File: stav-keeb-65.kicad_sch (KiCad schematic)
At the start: 0 parts

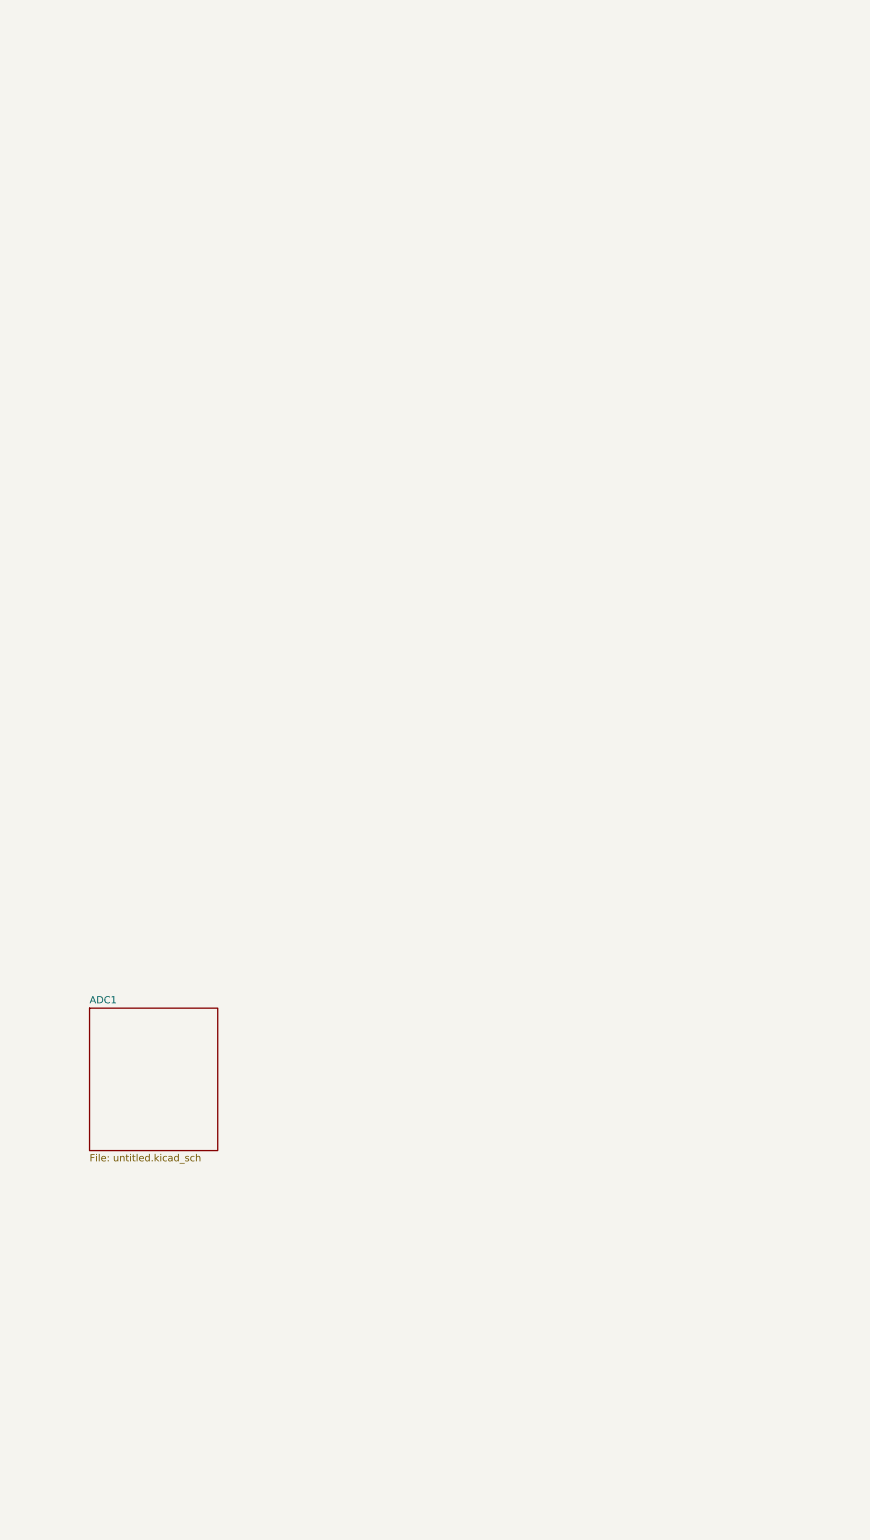
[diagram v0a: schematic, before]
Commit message: RP2040 initial draw
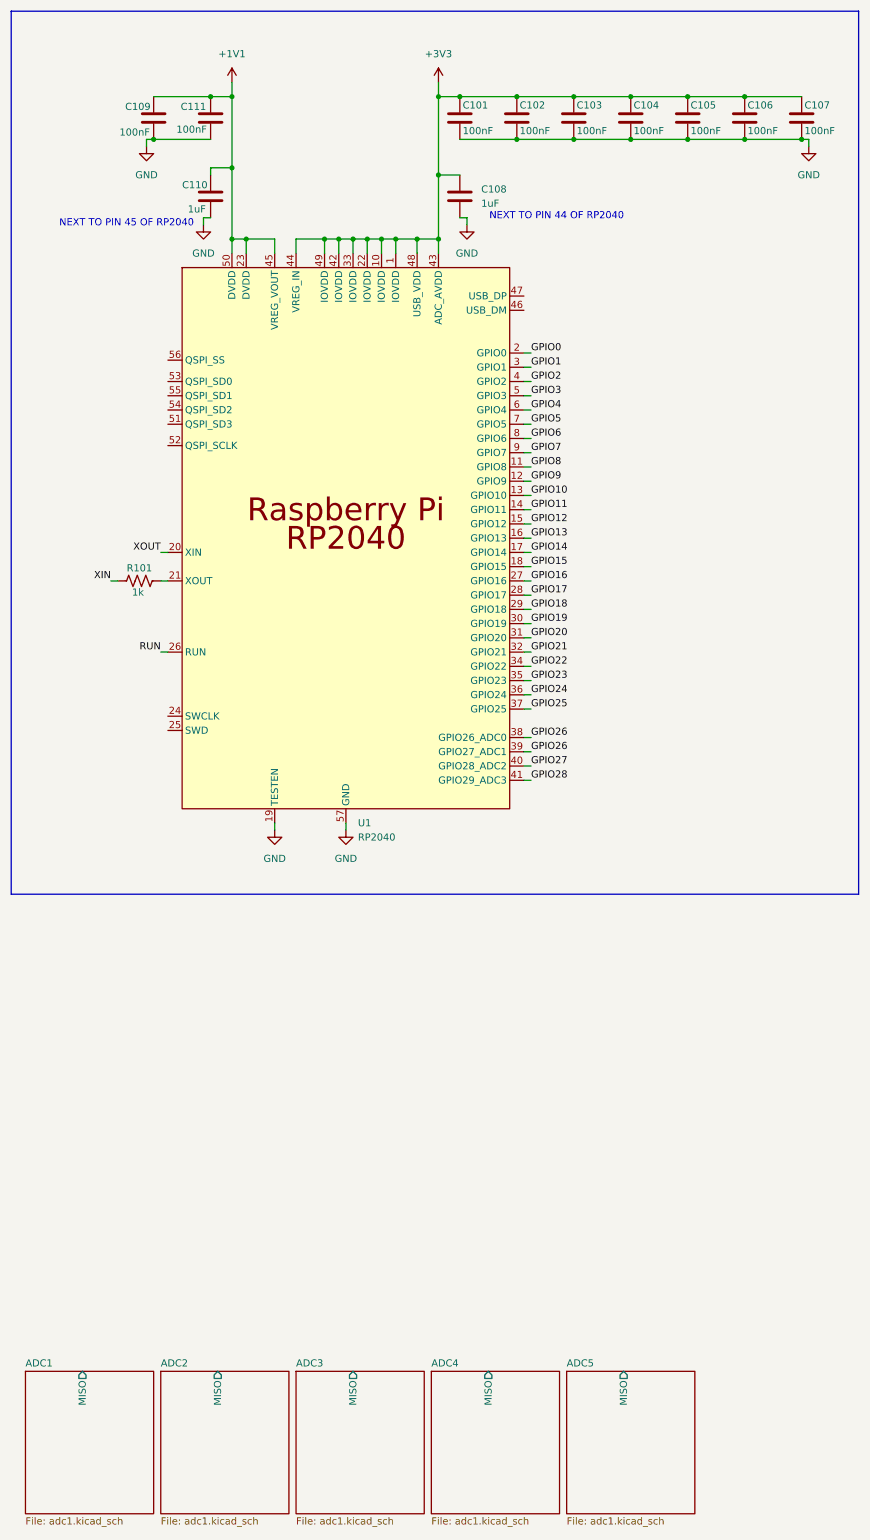
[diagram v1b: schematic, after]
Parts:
- added C101, C102, C103, C104, C105, C106, C107, C109, C111: 100nF, Capacitor_SMD:C_0201_0603Metric_Pad0.64x0.40mm_HandSolder, symbol Device:C
- added C108, C110: 1uF, Capacitor_SMD:C_0201_0603Metric_Pad0.64x0.40mm_HandSolder, symbol Device:C
- added R101: 1k, Capacitor_SMD:C_0201_0603Metric_Pad0.64x0.40mm_HandSolder, symbol Device:R_US
- added U1: RP2040, easyeda2kicad:LQFN-56_L7.0-W7.0-P0.4-EP, symbol easyeda2kicad:RP2040
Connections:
- new net: R101.2, U1.21 (XOUT)
- new net +1V1: C109.1, C110.1, C111.1, U1.23 (DVDD), U1.45 (VREG_VOUT), U1.50 (DVDD)
- new net +3V3: C101.1, C102.1, C103.1, C104.1, C105.1, C106.1, C107.1, C108.1, U1.1 (IOVDD), U1.10 (IOVDD), U1.22 (IOVDD), U1.33 (IOVDD), U1.42 (IOVDD), U1.43 (ADC_AVDD), U1.44 (VREG_IN), U1.48 (USB_VDD), U1.49 (IOVDD)
- new net GND: C101.2, C102.2, C103.2, C104.2, C105.2, C106.2, C107.2, C108.2, C109.2, C110.2, C111.2, U1.19 (TESTEN), U1.57 (GND)
- new net GPIO0: U1.2 (GPIO0)
- new net GPIO1: U1.3 (GPIO1)
- new net GPIO10: U1.13 (GPIO10)
- new net GPIO11: U1.14 (GPIO11)
- new net GPIO12: U1.15 (GPIO12)
- new net GPIO13: U1.16 (GPIO13)
- new net GPIO14: U1.17 (GPIO14)
- new net GPIO15: U1.18 (GPIO15)
- new net GPIO16: U1.27 (GPIO16)
- new net GPIO17: U1.28 (GPIO17)
- new net GPIO18: U1.29 (GPIO18)
- new net GPIO19: U1.30 (GPIO19)
- new net GPIO2: U1.4 (GPIO2)
- new net GPIO20: U1.31 (GPIO20)
- new net GPIO21: U1.32 (GPIO21)
- new net GPIO22: U1.34 (GPIO22)
- new net GPIO23: U1.35 (GPIO23)
- new net GPIO24: U1.36 (GPIO24)
- new net GPIO25: U1.37 (GPIO25)
- new net GPIO26: U1.38 (GPIO26_ADC0), U1.39 (GPIO27_ADC1)
- new net GPIO27: U1.40 (GPIO28_ADC2)
- new net GPIO28: U1.41 (GPIO29_ADC3)
- new net GPIO3: U1.5 (GPIO3)
- new net GPIO4: U1.6 (GPIO4)
- new net GPIO5: U1.7 (GPIO5)
- new net GPIO6: U1.8 (GPIO6)
- new net GPIO7: U1.9 (GPIO7)
- new net GPIO8: U1.11 (GPIO8)
- new net GPIO9: U1.12 (GPIO9)
- new net RUN: U1.26 (RUN)
- new net XIN: R101.1
- new net XOUT: U1.20 (XIN)
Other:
- added sheet ADC2 (adc1.kicad_sch)
- added sheet ADC3 (adc1.kicad_sch)
- added sheet ADC4 (adc1.kicad_sch)
- added sheet ADC5 (adc1.kicad_sch)
- sheet ADC1: file untitled.kicad_sch -> adc1.kicad_sch
- sheet ADC1 ports: added MISO; removed none
- note added: "NEXT TO PIN 44 OF RP2040"
- note added: "NEXT TO PIN 45 OF RP2040"
- title: (none) -> stav-keeb-65

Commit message: Oscillator and Flash
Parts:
- added C112: 100nF, Capacitor_SMD:C_0201_0603Metric_Pad0.64x0.40mm_HandSolder, symbol Device:C
- added C113, C114: 20pF, Capacitor_SMD:C_0201_0603Metric_Pad0.64x0.40mm_HandSolder, symbol Device:C
- added C115: 1uF, Capacitor_SMD:C_0201_0603Metric_Pad0.64x0.40mm_HandSolder, symbol Device:C
- added R102: 10k, Resistor_SMD:R_0201_0603Metric_Pad0.64x0.40mm_HandSolder, symbol Device:R_US
- added U7: ZD25D40CNJGR, easyeda2kicad:USON-8_L1.5-W1.5-P0.40-BL-EP, symbol easyeda2kicad:ZD25D40CNJGR
- added X1: X322512MSB4SI, easyeda2kicad:CRYSTAL-SMD_4P-L3.2-W2.5-BL, symbol easyeda2kicad:X322512MSB4SI
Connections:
- net +3V3: now also C115.1, R102.1
- net GND: now also C112.2, C113.2, C114.1, U7.4 (GND), U7.9 (EP), X1.2 (GND), X1.4 (GND)
- net RUN: now also C112.1, R102.2
- net XIN: now also C113.1, X1.3 (OSC2)
- net XOUT: now also C114.2, X1.1 (OSC1)
- net FLASH_SCLK: now reaches U1.52 (QSPI_SCLK)
- net FLASH_SCLK: now also U7.6 (SCLK)
- net FLASH_SD0: now reaches U1.53 (QSPI_SD0)
- net FLASH_SD0: now also U7.5 (SI)
- net FLASH_SD2: now reaches U1.54 (QSPI_SD2)
- net FLASH_SD2: now also U7.3 (~{WP})
- net FLASH_SD1: now reaches U1.55 (QSPI_SD1)
- net FLASH_SD1: now also U7.2 (SO)
- net FLASH_~{CS}: now reaches U1.56 (QSPI_SS)
- net FLASH_~{CS}: now also U7.1 (~{CS})
- new net: C115.2, U7.8 (VCC)
- no-connect marks 0 -> 2
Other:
- note added: "DO NOT POOR COPPER"

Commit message: RESET & BOOTSEL BUTTONS
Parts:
- added SW201: RESET, easyeda2kicad:SW-SMD_4P-L5.1-W5.1-P3.70-LS6.5-TL_H1.5, symbol easyeda2kicad:TS-1187A-B-A-B
- added SW202: BOOTSEL, easyeda2kicad:SW-SMD_4P-L5.1-W5.1-P3.70-LS6.5-TL_H1.5, symbol easyeda2kicad:TS-1187A-B-A-B
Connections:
- net FLASH_~{CS}: now also SW202.1 (A), SW202.2 (B)
- net GND: now also SW201.3 (C), SW201.4 (D), SW202.3 (C), SW202.4 (D)
- net RUN: now also SW201.1 (A), SW201.2 (B)

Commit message: Power & USB
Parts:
- added C116, C119, C120: 100nF, Capacitor_SMD:C_0603_1608Metric_Pad1.08x0.95mm_HandSolder, symbol Device:C
- added C117, C118: 10uF, Capacitor_SMD:C_1206_3216Metric_Pad1.33x1.80mm_HandSolder, symbol Device:C
- added C121: 22uF, Capacitor_SMD:C_1206_3216Metric_Pad1.33x1.80mm_HandSolder, symbol Device:C
- added C122: 4.7nF, Capacitor_SMD:C_0603_1608Metric_Pad1.08x0.95mm_HandSolder, symbol Device:C
- added C123, C124: 1nF, Capacitor_SMD:C_0603_1608Metric_Pad1.08x0.95mm_HandSolder, symbol Device:C
- added D1: SMF5.0A, easyeda2kicad:SOD-123F_L2.8-W1.8-LS3.7-RD, symbol easyeda2kicad:SMF5.0A_C151296
- added D2: USBLC6-2SC6, easyeda2kicad:SOT-23-6_L2.9-W1.6-P0.95-LS2.8-BL, symbol easyeda2kicad:USBLC6-2SC6
- added F1: Littelfuse 1812L110/33MR, symbol Device:Fuse
- added FB1: TDK MPZ2012S101AT000, symbol Device:FerriteBead
- added R103, R104: 5.1k, Resistor_SMD:R_0603_1608Metric_Pad0.98x0.95mm_HandSolder, symbol Device:R_US
- added R105: 1M, Resistor_SMD:R_0603_1608Metric_Pad0.98x0.95mm_HandSolder, symbol Device:R_US
- added R106, R107: 100k, Resistor_SMD:R_0603_1608Metric_Pad0.98x0.95mm_HandSolder, symbol Device:R_US
- added U8: RT9013-33GB, easyeda2kicad:SOT-23-5_L3.0-W1.7-P0.95-LS2.8-BL, symbol easyeda2kicad:RT9013-33GB
- added USBC1: TYPE-C-31-M-12, easyeda2kicad:USB-C_SMD-TYPE-C-31-M-12_1, symbol easyeda2kicad:TYPE-C-31-M-12
- C101, C102, C103, C104, C105, C106, C107, C108, C109, C110, C111, C112, C113, C114, C115, R101: footprint Capacitor_SMD:C_0201_0603Metric_Pad0.64x0.40mm_HandSolder -> Capacitor_SMD:C_0603_1608Metric_Pad1.08x0.95mm_HandSolder
- R102: footprint Resistor_SMD:R_0201_0603Metric_Pad0.64x0.40mm_HandSolder -> Capacitor_SMD:C_0603_1608Metric_Pad1.08x0.95mm_HandSolder
- renumbered SW201 to _SW201, SW202 to _SW202
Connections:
- net +3V3: now also C116.1, C117.1, U8.5 (VOUT)
- net GND: now also C116.2, C117.2, C118.2, C119.2, C120.2, C121.2, C122.2, C123.1, C124.2, D1.2, D2.2, R103.2, R105.2, U8.2 (GND), USBC1.A1B12 (GND), USBC1.B1A12 (GND)
- net GPIO26: now also C123.2, R107.1; no longer U1.39 (GPIO27_ADC1)
- net GPIO27: now also U1.39 (GPIO27_ADC1), C124.1, R106.1; no longer U1.40 (GPIO28_ADC2)
- net GPIO28: now also U1.40 (GPIO28_ADC2); no longer U1.41 (GPIO29_ADC3)
- new net: R103.1, R107.2, USBC1.A5 (CC1)
- new net: R104.1, R106.2, USBC1.B5 (CC2)
- new net: C122.1, R105.1, USBC1.1 (EH), USBC1.2 (EH), USBC1.3 (EH), USBC1.4 (EH)
- new net GPIO29: U1.41 (GPIO29_ADC3)
- new net USB_D1N: D2.3, USBC1.A7 (DN1), USBC1.B7 (DN2)
- new net USB_D1P: D2.1, USBC1.A6 (DP1), USBC1.B6 (DP2)
- new net USB_DN: D2.4
- new net USB_DP: D2.6
- new net VBUS: D1.1, D2.5, F1.1, USBC1.A4B9 (VBUS), USBC1.B4A9 (VBUS)
- new net V_Filtered: C120.1, C121.1, FB1.2
- new net V_Fused: C118.1, C119.1, F1.2, FB1.1, U8.1 (VIN), U8.3 (EN)
- no-connect marks 2 -> 5

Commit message: USB connection to RP2040
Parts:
- added R108, R109: 22, Resistor_SMD:R_0603_1608Metric_Pad0.98x0.95mm_HandSolder, symbol Device:R_US
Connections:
- net USB_DN: now also R109.1
- net USB_DP: now also R108.1
- net at U1.46 (USB_DN): now also R109.2
- net at U1.47 (USB_DP): now also R108.2

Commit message: 2.5V ref
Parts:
- added C125: 10nF, Capacitor_SMD:C_0603_1608Metric_Pad1.08x0.95mm_HandSolder, symbol Device:C
- added C126: 1uF, Capacitor_SMD:C_0603_1608Metric_Pad1.08x0.95mm_HandSolder, symbol Device:C
- added C127, C129: 100nF, Capacitor_SMD:C_0603_1608Metric_Pad1.08x0.95mm_HandSolder, symbol Device:C
- added C128: 10uF, Capacitor_SMD:C_1206_3216Metric_Pad1.33x1.80mm_HandSolder, symbol Device:C
- added R110: 10, Resistor_SMD:R_0603_1608Metric_Pad0.98x0.95mm_HandSolder, symbol Device:R_US
- added R111, R112: 10k 0.1%, Resistor_SMD:R_0603_1608Metric_Pad0.98x0.95mm_HandSolder, symbol Device:R_US
- added U9: OPA320AIDBVR, easyeda2kicad:SOT-23-5_L3.0-W1.7-P0.95-LS2.8-BR, symbol easyeda2kicad:OPA320AIDBVR
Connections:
- net GND: now also C125.2, C126.2, C127.1, C128.2, C129.1, R112.2, U9.2 (V-)
- net V_Filtered renamed +5VA
- net +5VA: now also C126.1, C129.2, R111.1, U9.5 (V+)
- new net: C125.1, R111.2, R112.1, U9.3 (IN+)
- new net: R110.1, U9.1 (OUT), U9.4 (IN-)
- new net +2V5_RREF: C127.2, C128.1, R110.2
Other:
- note added: "ADC"
- note added: "Buttons"
- note added: "Flash"
- note added: "Microcontroller"
- note added: "Oscillator"
- note added: "Power"
- note added: "USB"

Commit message: Change 2.5V ref to voltage divider
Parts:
- removed U7: ZD25D40CNJGR, easyeda2kicad:USON-8_L1.5-W1.5-P0.40-BL-EP, symbol easyeda2kicad:ZD25D40CNJGR
- added C135: 100nF, Capacitor_SMD:C_0603_1608Metric_Pad1.08x0.95mm_HandSolder, symbol Device:C
- added R113: 1k, Resistor_SMD:R_0603_1608Metric_Pad0.98x0.95mm_HandSolder, symbol Device:R_US
- added R114: 10k, Resistor_SMD:R_0603_1608Metric_Pad0.98x0.95mm_HandSolder, symbol Device:R_US
- added U7: W25Q128JVSIQTR, easyeda2kicad:SOIC-8_L5.3-W5.3-P1.27-LS8.0-BL, symbol easyeda2kicad:W25Q128JVSIQTR
- R101, R102: footprint Capacitor_SMD:C_0603_1608Metric_Pad1.08x0.95mm_HandSolder -> Resistor_SMD:R_0603_1608Metric_Pad0.98x0.95mm_HandSolder
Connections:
- net +3V3: now also C135.1, R114.1
- net FLASH_SCLK: now also U7.6 (CLK)
- net FLASH_SD0: now also U7.5 (DI)
- net FLASH_SD1: now also U7.2 (DO)
- net FLASH_SD2: now also U7.3 (IO2)
- net FLASH_~{CS}: now also R113.1, R114.2, U7.1 (~{CS}); no longer _SW202.1 (A), _SW202.2 (B)
- net GND: now also U7.4 (GND)
- net at C115.2: now also C135.2, U7.8 (VCC)
- net FLASH_SD3: now reaches U1.51 (QSPI_SD3)
- net FLASH_SD3: now also U7.7 (IO3)
- new net: R113.2, _SW202.1 (A), _SW202.2 (B)
- no-connect marks 5 -> 3
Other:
- moved on the sheet: _SW201, _SW202

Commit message: ERC fixes
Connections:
- net GND: now also R104.2
- no-connect marks 3 -> 5
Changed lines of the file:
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@@
+	)
+	(no_connect
+		(at 40.64 140.97)
 	)
 	(no_connect
@@
 		(at 287.02 57.15)
 	)
+	(no_connect
+		(at 40.64 138.43)
+	)
 	(wire
 		(pts
@@
 		)
 		(stroke
+			(width 0)
+			(type default)
+		)
+	)
+	(wire
+		(pts
+			(xy 250.19 127) (xy 250.19 128.27)
+		)
+		(stroke
